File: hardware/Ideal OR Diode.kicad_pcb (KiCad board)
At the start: 2 copper layers, 38.9 x 44.9 mm, 18 parts, among them J1 PWR A, J2 PWR B, J3 PWR OUT, J4 Conn_01x03_Pin, Q1 BSC030N03LS_G, Q2 BSC030N03LS_G, Q3 BSC030N03LS_G, Q4 BSC030N02LS_G, U1 LTC4353IMS

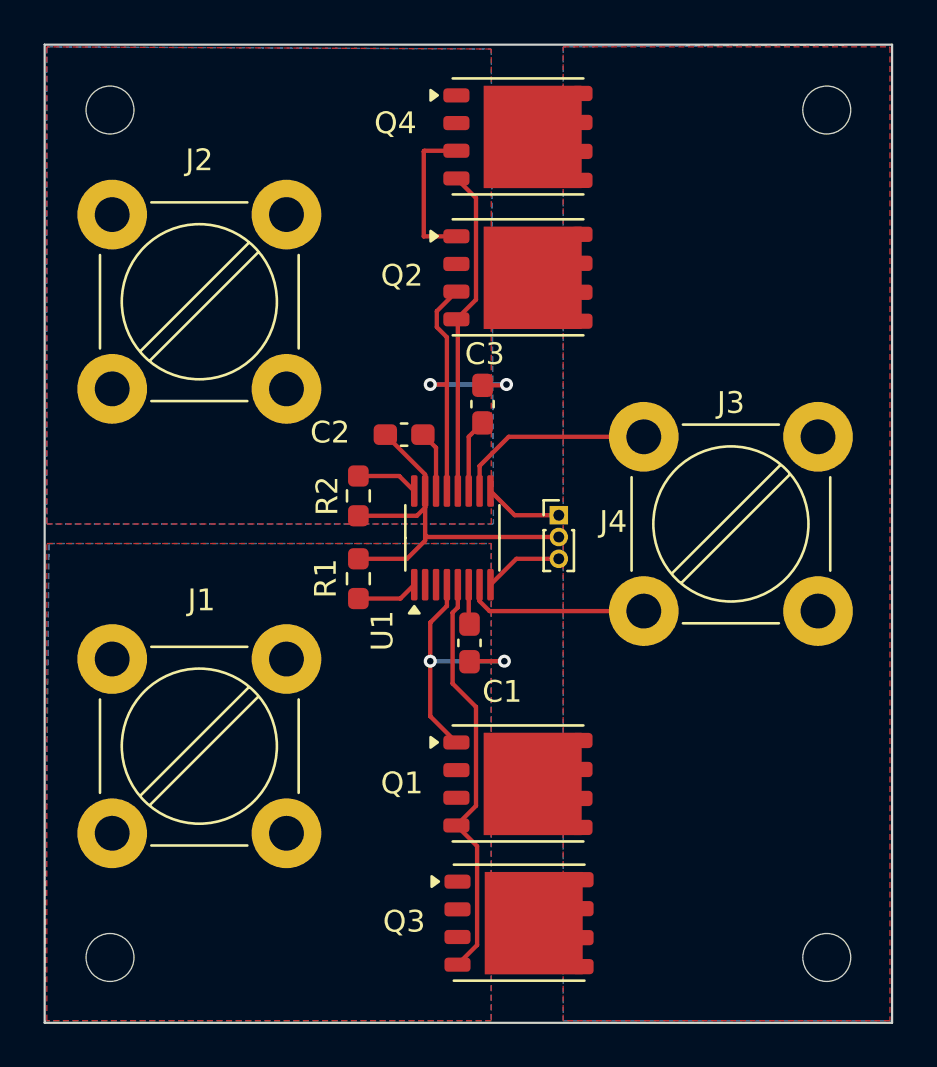
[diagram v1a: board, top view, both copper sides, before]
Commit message: Update via-stiching
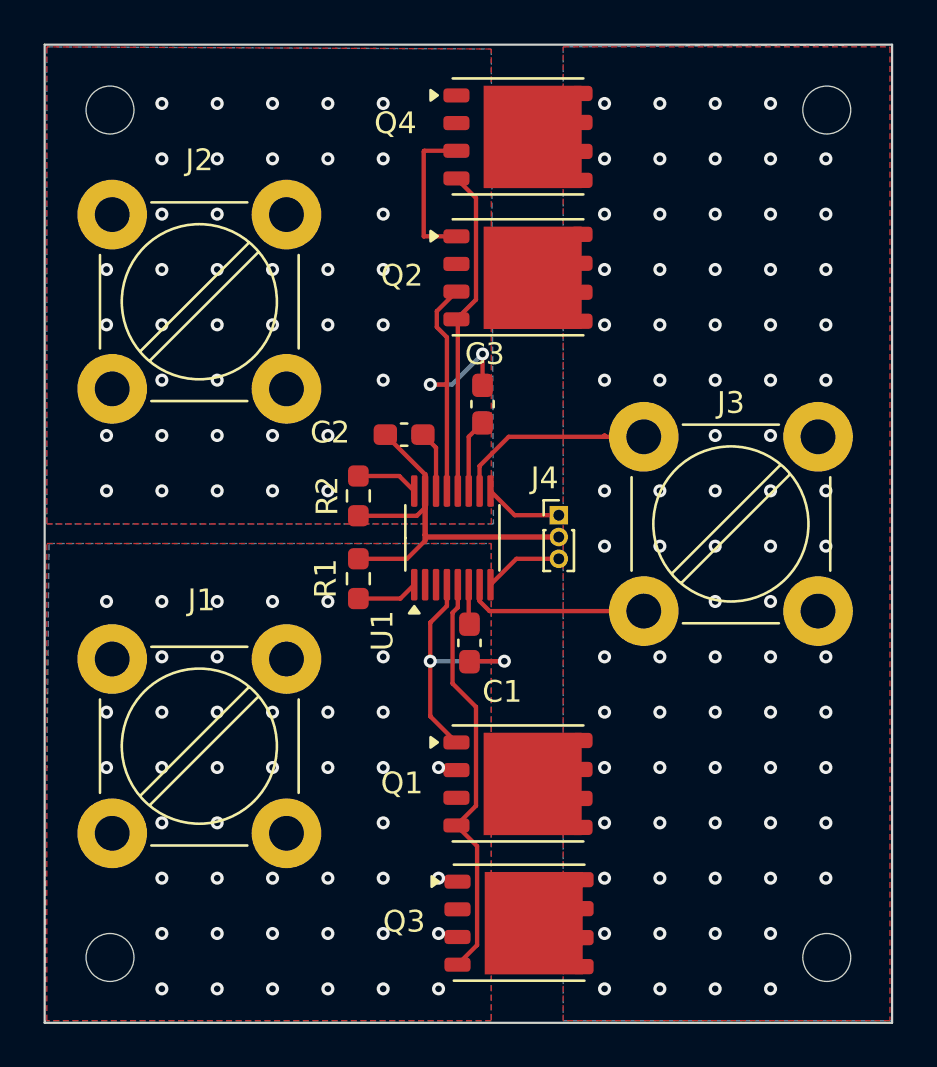
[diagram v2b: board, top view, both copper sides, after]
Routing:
- net +12B: track 22.2 -> 21.8 mm, vias 2 -> 40
- net +12V: track 17.7 -> 17.8 mm, vias 0 -> 76
- net +12A: vias 2 -> 44
